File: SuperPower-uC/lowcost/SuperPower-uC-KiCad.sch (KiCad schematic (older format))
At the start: 0 parts

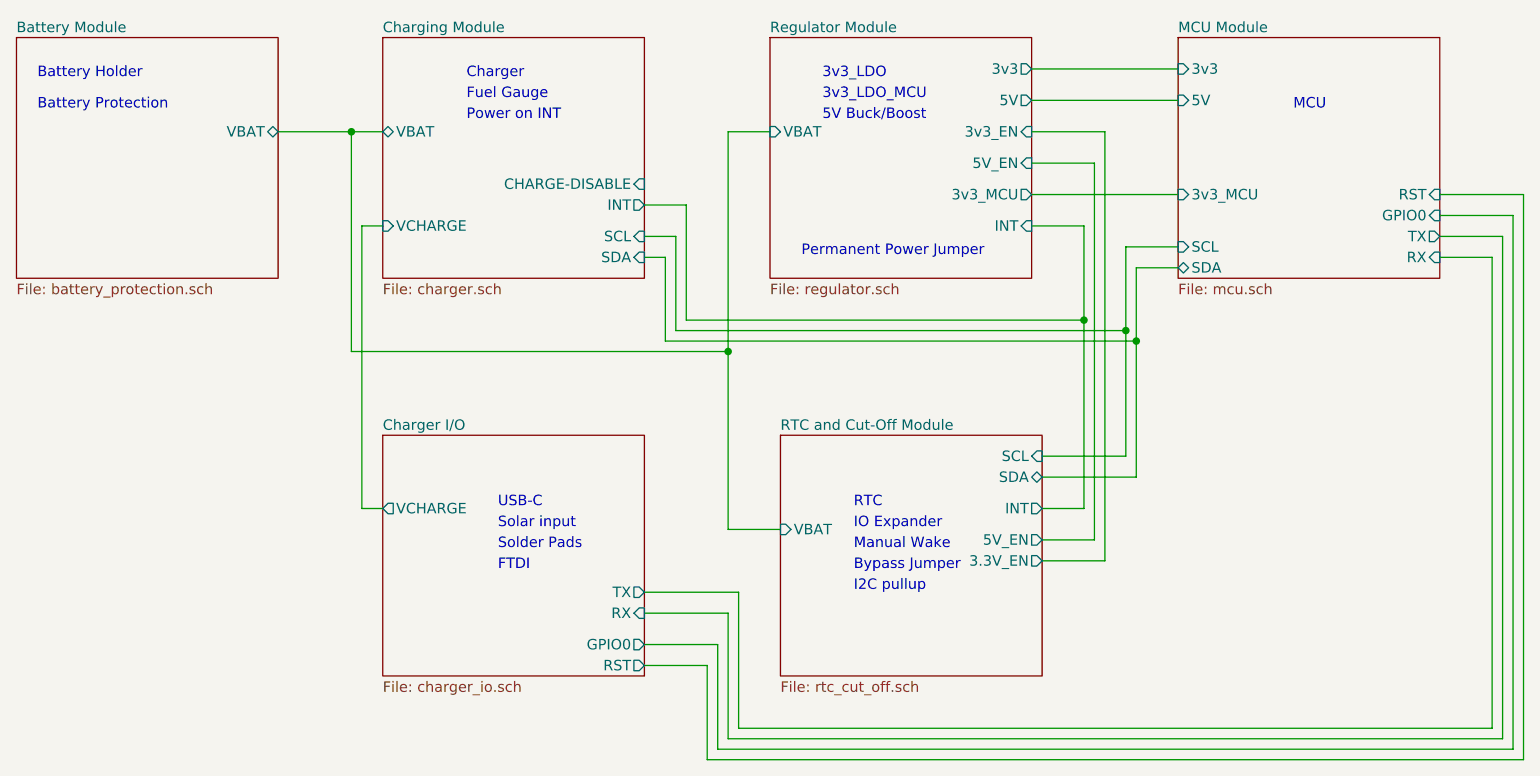
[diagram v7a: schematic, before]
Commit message: added charge disable connection
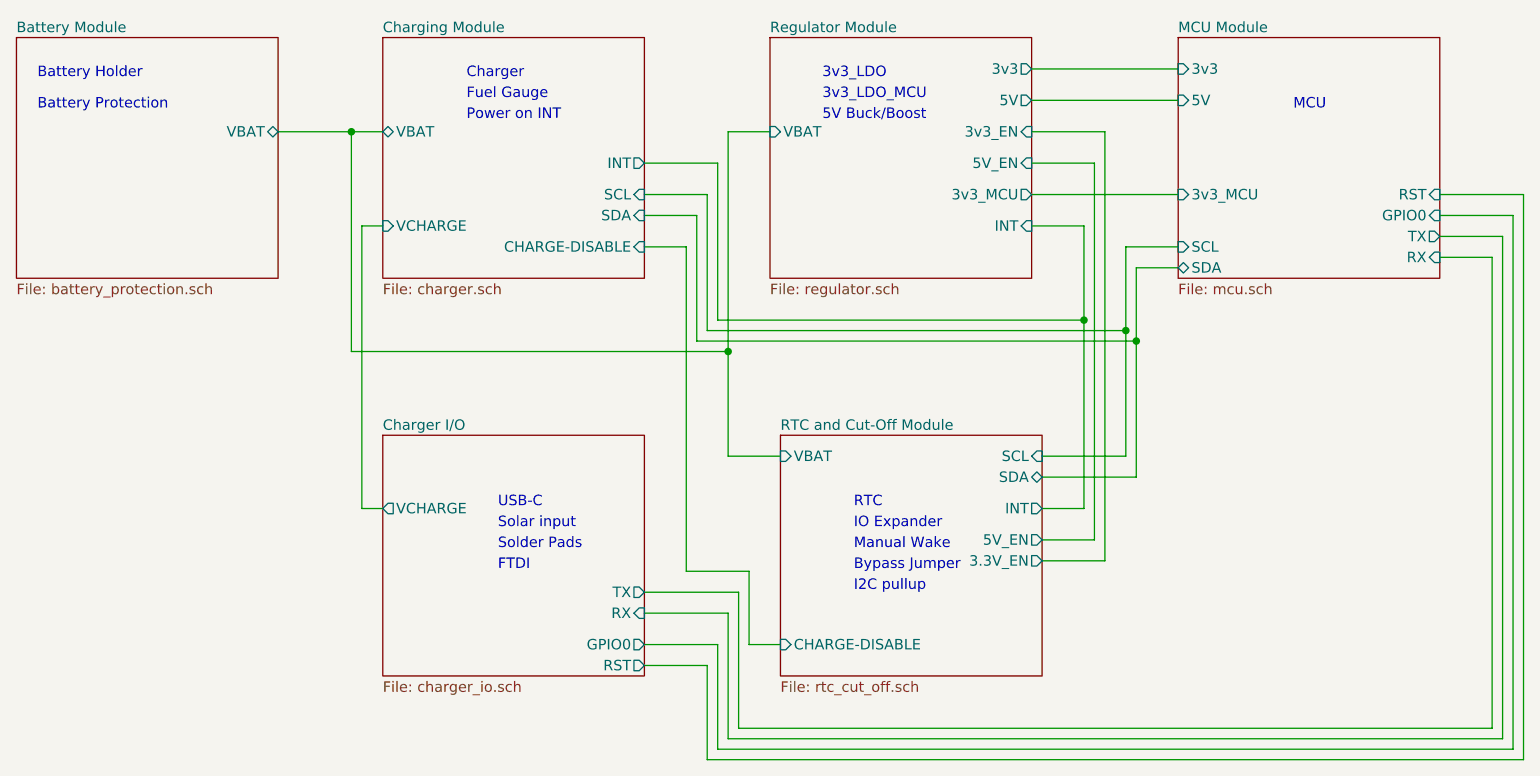
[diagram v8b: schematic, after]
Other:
- note removed: "Permanent Power Jumper"
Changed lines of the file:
@@
 F0 "Charging Module" 50
 F1 "charger.sch" 50
-F2 "SCL" I R 4300 3050 50
-F3 "SDA" I R 4300 3150 50
-F4 "INT" O R 4300 2900 50
+F2 "SCL" I R 4300 2850 50
+F3 "SDA" I R 4300 2950 50
+F4 "INT" O R 4300 2700 50
 F5 "VCHARGE" I L 3050 3000 50
-F6 "CHARGE-DISABLE" I R 4300 2800 50
+F6 "CHARGE-DISABLE" I R 4300 3100 50
 F7 "VBAT" B L 3050 2550 50
 $EndSheet
@@
 F3 "SDA" B R 6200 4200 50
 F4 "INT" O R 6200 4350 50
-F5 "VBAT" I L 4950 4450 50
+F5 "VBAT" I L 4950 4100 50
 F6 "3.3V_EN" O R 6200 4600 50
 F7 "5V_EN" O R 6200 4500 50
+F8 "CHARGE-DISABLE" I L 4950 5000 50
 $EndSheet
 $Sheet
@@
 	6600 4100 6200 4100
 Wire Wire Line
-	4950 4450 4700 4450
-Wire Wire Line
-	4700 4450 4700 3600
+	4950 4100 4700 4100
+Wire Wire Line
+	4700 4100 4700 3600
 Wire Wire Line
 	4700 2550 4900 2550
@@
 Solder Pads
 Wire Wire Line
-	4300 3050 4450 3050
-Wire Wire Line
-	4450 3050 4450 3500
-Wire Wire Line
-	4450 3500 6600 3500
+	4300 2850 4600 2850
+Wire Wire Line
+	4600 2850 4600 3500
+Wire Wire Line
+	4600 3500 6600 3500
 Connection ~ 6600 3500
 Wire Wire Line
 	6600 3500 6600 4100
 Wire Wire Line
-	4300 3150 4400 3150
-Wire Wire Line
-	4400 3150 4400 3550
-Wire Wire Line
-	4400 3550 6650 3550
+	4300 2950 4550 2950
+Wire Wire Line
+	4550 2950 4550 3550
+Wire Wire Line
+	4550 3550 6650 3550
 Connection ~ 6650 3550
 Wire Wire Line
@@
 Wire Wire Line
 	8400 5450 4700 5450
-Text Notes 5050 3150 0    50   ~ 0
-Permanent Power Jumper
 Text Notes 5300 4650 0    50   ~ 0
 Bypass Jumper
@@
 	6400 3000 6150 3000
 Wire Wire Line
-	4300 2900 4500 2900
-Wire Wire Line
-	4500 2900 4500 3450
-Wire Wire Line
-	4500 3450 6400 3450
+	4300 2700 4650 2700
+Wire Wire Line
+	4650 2700 4650 3450
+Wire Wire Line
+	4650 3450 6400 3450
 Connection ~ 6400 3450
 Wire Wire Line
@@
 Wire Wire Line
 	6150 2400 6850 2400
+Wire Wire Line
+	4300 3100 4500 3100
+Wire Wire Line
+	4500 3100 4500 4650
+Wire Wire Line
+	4500 4650 4800 4650
+Wire Wire Line
+	4800 4650 4800 5000
+Wire Wire Line
+	4800 5000 4950 5000
 $EndSCHEMATC
